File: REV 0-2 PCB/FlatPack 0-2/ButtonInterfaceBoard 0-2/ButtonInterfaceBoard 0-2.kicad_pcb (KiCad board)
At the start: 2 copper layers, 36.8 x 47 mm, 36 parts, among them J1 Conn_01x03, J2 Conn_01x02, J3 Conn_01x05, J4 Conn_01x04, J5 Conn_01x03, J6 Conn_01x03, J7 AVR-ISP-6, J8 Conn_01x02, J9 Conn_01x04, U1 W25Q16JVSSIQ, U2 ATA6561, U3 ATtiny24A-SSU

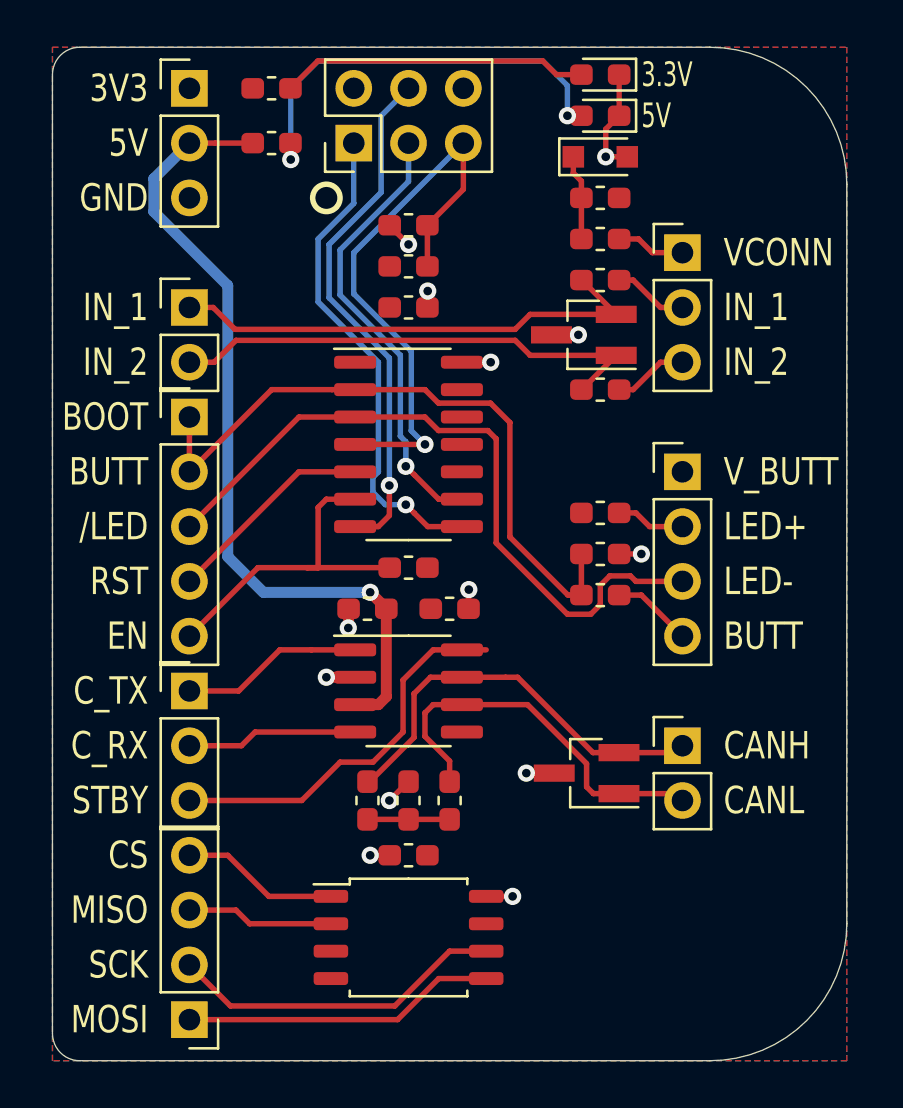
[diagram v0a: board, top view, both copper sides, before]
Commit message: Fixing working tree, pushing a bunch of SubBoards and FlatPack BOM
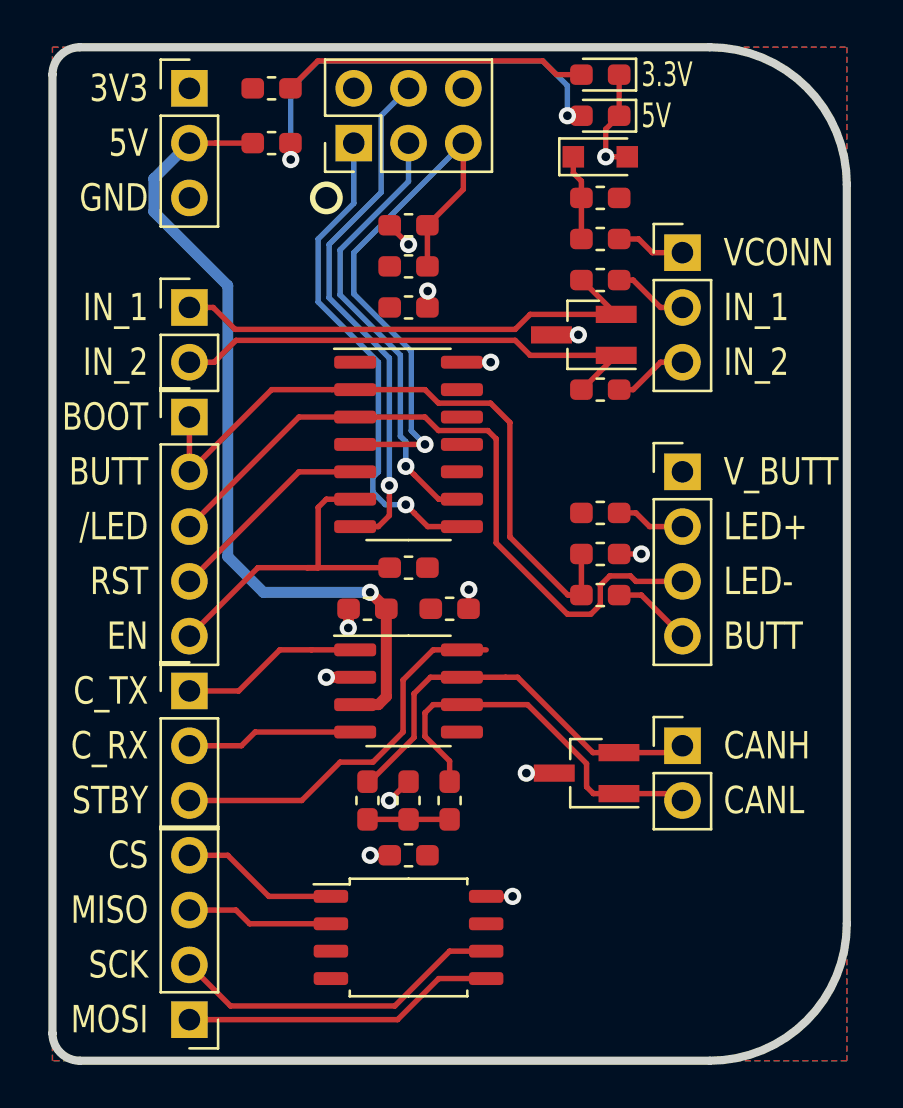
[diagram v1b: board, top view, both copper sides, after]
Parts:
- R12: value 120R -> 100R
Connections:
- U3 pad 10: Net-(U3-Pad10) -> (no net)
- U3 pad 11: Net-(U3-Pad11) -> (no net)
- U3 pad 12: Net-(U3-Pad12) -> (no net)
- U3 pad 13: Net-(U3-Pad13) -> (no net)
